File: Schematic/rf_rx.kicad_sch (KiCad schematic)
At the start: 12 parts, among them SW2 TS24CA, U1 ME6217C33M5G, U12 ESP-01F-2M, U13 E28-2G4M27SX

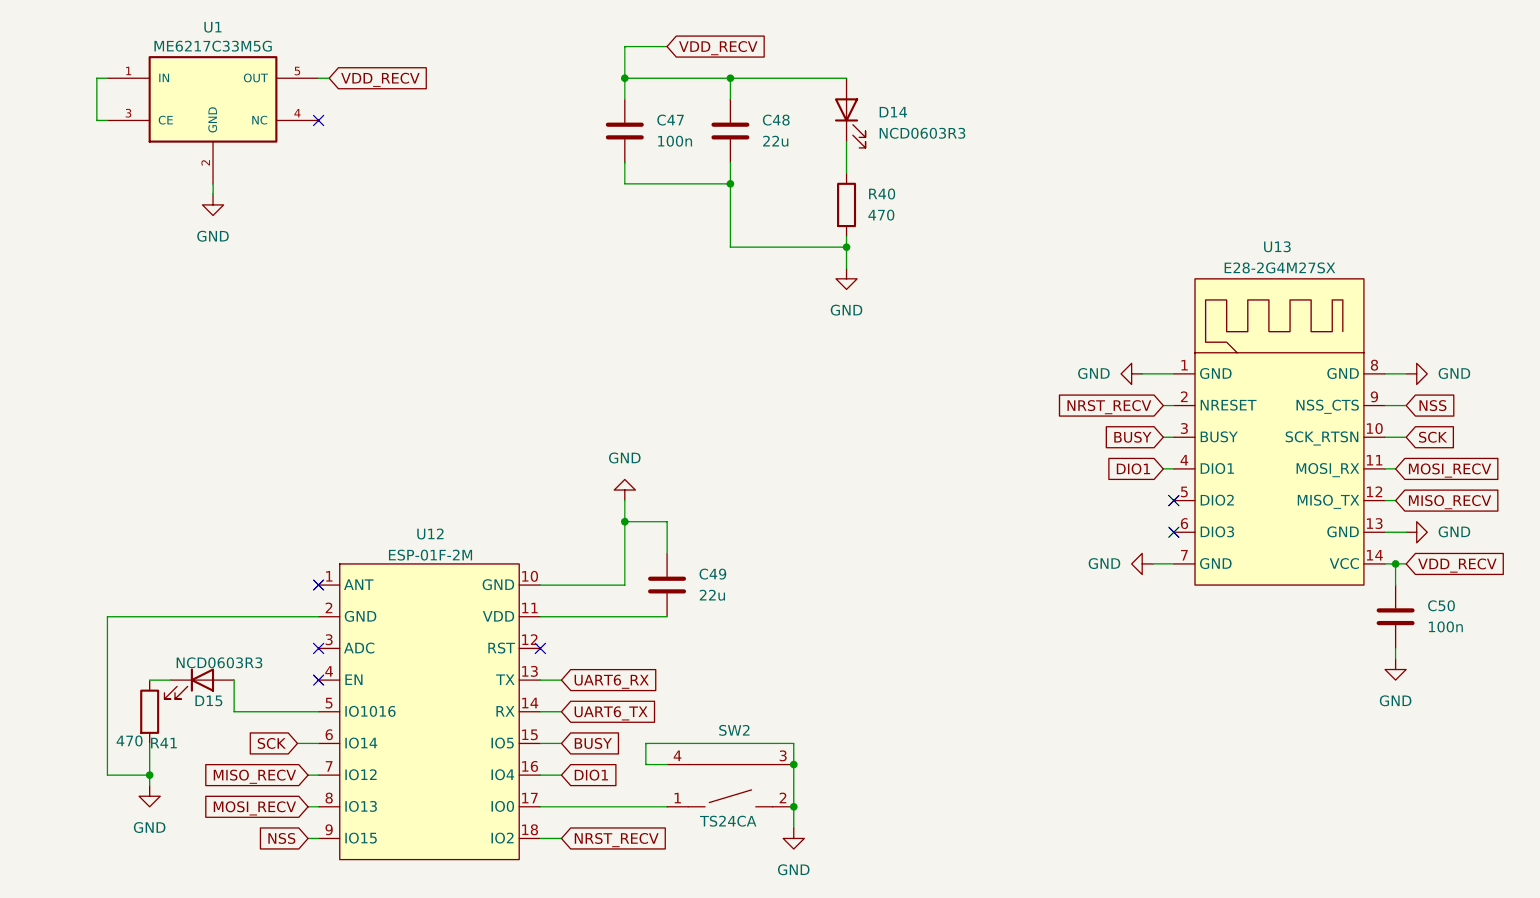
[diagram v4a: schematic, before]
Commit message: Refactor schematic files and update component placements
- Adjusted component positions in osd.kicad_sch for better layout.
- Added new junctions and wires in rf_rx.kicad_sch to improve connectivity.
- Introduced additional junctions and wires in sensors.kicad_sch for enhanced signal routing.
- Removed outdated backup file fch7-2025-11-18_191836.zip and added new backup fch7-2025-11-27_202230.zip.
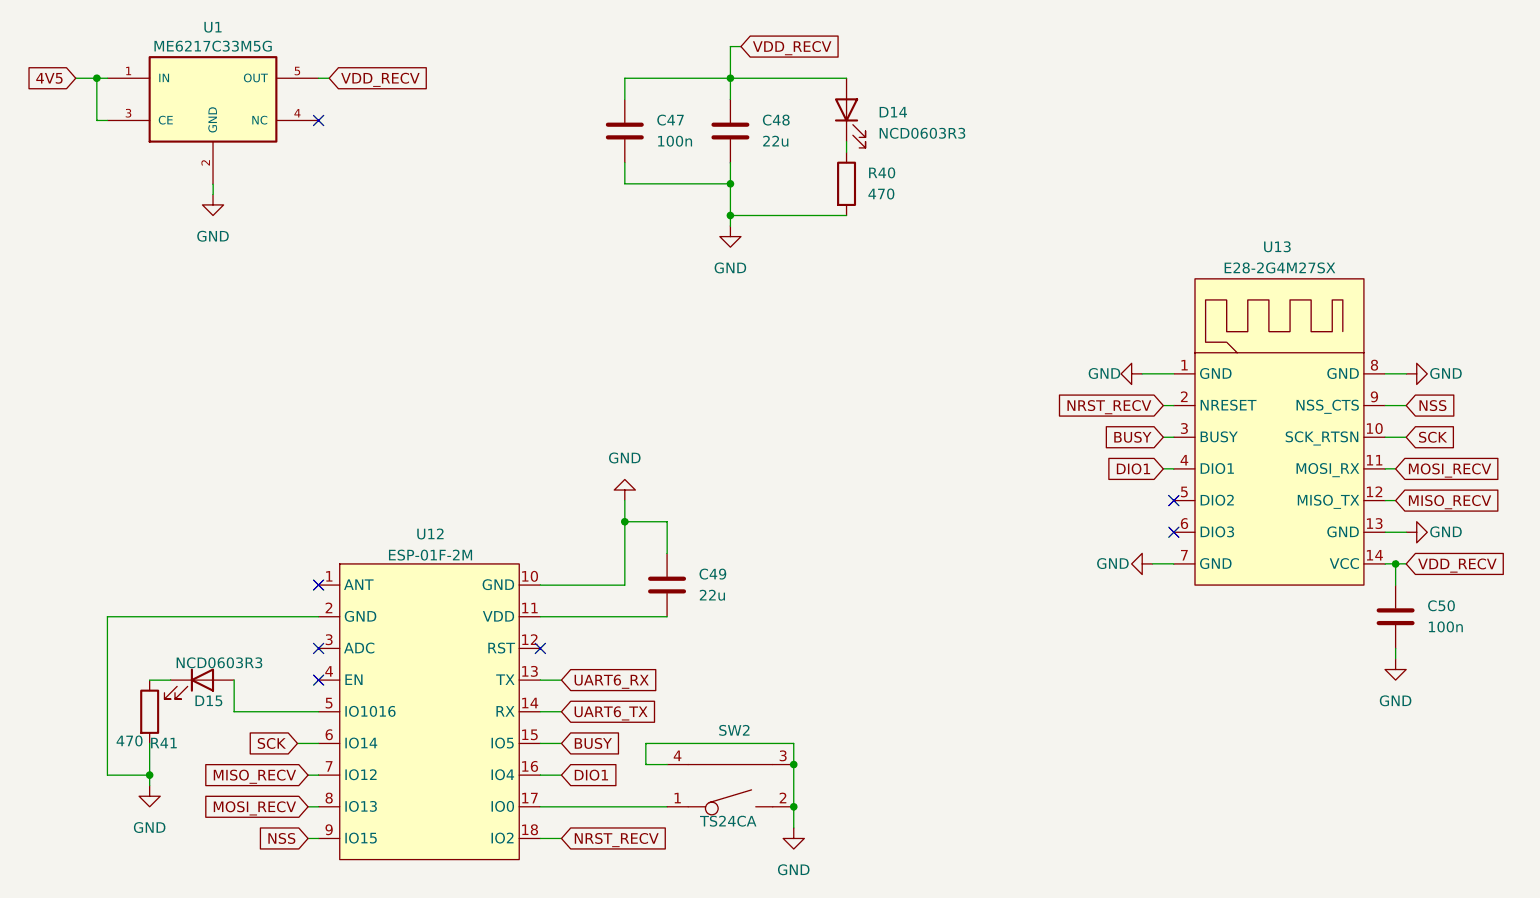
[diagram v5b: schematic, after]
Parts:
- SW2: footprint fch7_fp:SW-SMD_2P-TS24CA -> ProLib_pcs_2025-11-24:SW-SMD_2P-TS24CA
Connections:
- net 4V5: now reaches U1.1 (IN), U1.3 (CE)
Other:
- moved on the sheet: R40
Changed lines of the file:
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@@
 	(paper "A4")
+	(junction
+		(at 57.15 66.04)
+		(diameter 0)
+		(color 0 0 0 0)
+	)
+	(junction
+		(at 120.65 119.38)
+		(diameter 0)
+		(color 0 0 0 0)
+	)
+	(junction
+		(at 63.5 149.86)
+		(diameter 0)
+		(color 0 0 0 0)
+	)
+	(junction
+		(at 133.35 66.04)
+		(diameter 0)
+		(color 0 0 0 0)
+	)
+	(junction
+		(at 140.97 148.59)
+		(diameter 0)
+		(color 0 0 0 0)
+	)
+	(junction
+		(at 140.97 153.67)
+		(diameter 0)
+		(color 0 0 0 0)
+	)
+	(junction
+		(at 133.35 82.55)
+		(diameter 0)
+		(color 0 0 0 0)
+	)
+	(junction
+		(at 213.36 124.46)
+		(diameter 0)
+		(color 0 0 0 0)
+	)
 	(junction
 		(at 133.35 78.74)
@@
 		(color 0 0 0 0)
 	)
-	(junction
-		(at 147.32 86.36)
-		(diameter 0)
-		(color 0 0 0 0)
-	)
-	(junction
-		(at 120.65 119.38)
-		(diameter 0)
-		(color 0 0 0 0)
-	)
-	(junction
-		(at 63.5 149.86)
-		(diameter 0)
-		(color 0 0 0 0)
-	)
-	(junction
-		(at 133.35 66.04)
-		(diameter 0)
-		(color 0 0 0 0)
-	)
-	(junction
-		(at 120.65 66.04)
-		(diameter 0)
-		(color 0 0 0 0)
-	)
-	(junction
-		(at 140.97 148.59)
-		(diameter 0)
-		(color 0 0 0 0)
-	)
-	(junction
-		(at 140.97 153.67)
-		(diameter 0)
-		(color 0 0 0 0)
-	)
-	(junction
-		(at 213.36 124.46)
-		(diameter 0)
-		(color 0 0 0 0)
-	)
 	(no_connect
 		(at 110.49 134.62)
@@
 	(wire
 		(pts
-			(xy 133.35 78.74) (xy 133.35 86.36)
-		)
-		(stroke
-			(width 0)
-			(type default)
-		)
-	)
-	(wire
-		(pts
 			(xy 120.65 76.2) (xy 120.65 78.74)
 		)
@@
 	(wire
 		(pts
+			(xy 133.35 62.23) (xy 133.35 66.04)
+		)
+		(stroke
+			(width 0)
+			(type default)
+		)
+	)
+	(wire
+		(pts
 			(xy 82.55 149.86) (xy 83.82 149.86)
 		)
@@
 	(wire
 		(pts
-			(xy 147.32 85.09) (xy 147.32 86.36)
-		)
-		(stroke
-			(width 0)
-			(type default)
-		)
-	)
-	(wire
-		(pts
-			(xy 147.32 86.36) (xy 147.32 88.9)
+			(xy 134.62 62.23) (xy 133.35 62.23)
 		)
 		(stroke
@@
 	(wire
 		(pts
+			(xy 147.32 73.66) (xy 147.32 74.93)
+		)
+		(stroke
+			(width 0)
+			(type default)
+		)
+	)
+	(wire
+		(pts
 			(xy 57.15 66.04) (xy 57.15 71.12)
 		)
@@
 	(wire
 		(pts
-			(xy 125.73 62.23) (xy 120.65 62.23)
-		)
-		(stroke
-			(width 0)
-			(type default)
-		)
-	)
-	(wire
-		(pts
-			(xy 147.32 73.66) (xy 147.32 77.47)
-		)
-		(stroke
-			(width 0)
-			(type default)
-		)
-	)
-	(wire
-		(pts
 			(xy 82.55 153.67) (xy 83.82 153.67)
 		)
@@
 	(wire
 		(pts
+			(xy 133.35 82.55) (xy 133.35 78.74)
+		)
+		(stroke
+			(width 0)
+			(type default)
+		)
+	)
+	(wire
+		(pts
+			(xy 54.61 66.04) (xy 57.15 66.04)
+		)
+		(stroke
+			(width 0)
+			(type default)
+		)
+	)
+	(wire
+		(pts
 			(xy 212.09 109.22) (xy 214.63 109.22)
 		)
@@
 	(wire
 		(pts
-			(xy 133.35 86.36) (xy 147.32 86.36)
-		)
-		(stroke
-			(width 0)
-			(type default)
-		)
-	)
-	(wire
-		(pts
 			(xy 185.42 113.03) (xy 186.69 113.03)
 		)
@@
 	(wire
 		(pts
-			(xy 120.65 62.23) (xy 120.65 66.04)
-		)
-		(stroke
-			(width 0)
-			(type default)
-		)
-	)
-	(wire
-		(pts
 			(xy 110.49 138.43) (xy 113.03 138.43)
 		)
@@
 	(wire
 		(pts
+			(xy 147.32 82.55) (xy 133.35 82.55)
+		)
+		(stroke
+			(width 0)
+			(type default)
+		)
+	)
+	(wire
+		(pts
 			(xy 125.73 123.19) (xy 125.73 119.38)
 		)
@@
 		(pts
 			(xy 140.97 148.59) (xy 140.97 153.67)
+		)
+		(stroke
+			(width 0)
+			(type default)
+		)
+	)
+	(wire
+		(pts
+			(xy 133.35 82.55) (xy 133.35 83.82)
 		)
 		(stroke
@@
 		)
 	)
+	(global_label "4V5"
+		(shape input)
+		(at 54.61 66.04 180)
+		(fields_autoplaced yes)
+		(effects
+			(font
+				(size 1.27 1.27)
+			)
+			(justify right)
+		)
+		(property "Intersheetrefs" "${INTERSHEET_REFS}"
+			(at 48.1172 66.04 0)
+			(effects
+				(font
+					(size 1.27 1.27)
+				)
+				(justify right)
+				(hide yes)
+			)
+		)
+	)
 	(global_label "MOSI_RECV"
 		(shape input)
@@
 	(global_label "VDD_RECV"
 		(shape input)
-		(at 125.73 62.23 0)
+		(at 134.62 62.23 0)
 		(fields_autoplaced yes)
 		(effects
@@
 		)
 		(property "Intersheetrefs" "${INTERSHEET_REFS}"
-			(at 138.089 62.23 0)
+			(at 146.979 62.23 0)
 			(effects
 				(font
@@
 		(on_board yes)
 		(dnp no)
-		(fields_autoplaced yes)
 		(property "Reference" "#PWR048"
 			(at 177.8 124.46 0)
@@
 		)
 		(property "Value" "GND"
-			(at 180.34 124.4599 90)
+			(at 181.356 124.46 90)
 			(effects
 				(font
@@
 		(on_board yes)
 		(dnp no)
-		(fields_autoplaced yes)
 		(property "Reference" "#PWR047"
 			(at 176.53 101.6 0)
@@
 		)
 		(property "Value" "GND"
-			(at 179.07 101.5999 90)
+			(at 180.34 101.6 90)
 			(effects
 				(font
@@
 		(on_board yes)
 		(dnp no)
-		(fields_autoplaced yes)
 		(property "Reference" "#PWR050"
 			(at 220.98 101.6 0)
@@
 		)
 		(property "Value" "GND"
-			(at 218.44 101.5999 90)
+			(at 217.424 101.6 90)
 			(effects
 				(font
@@
 			)
 		)
-		(property "Footprint" "fch7_fp:SW-SMD_2P-TS24CA"
+		(property "Footprint" "ProLib_pcs_2025-11-24:SW-SMD_2P-TS24CA"
 			(at 132.588 144.526 0)
 			(effects
@@
 	(symbol
 		(lib_id "power:GND")
-		(at 147.32 88.9 0)
+		(at 133.35 83.82 0)
 		(unit 1)
 		(exclude_from_sim no)
@@
 		(fields_autoplaced yes)
 		(property "Reference" "#PWR043"
-			(at 147.32 95.25 0)
+			(at 133.35 90.17 0)
 			(effects
 				(font
@@
 		)
 		(property "Value" "GND"
-			(at 147.32 93.98 0)
+			(at 133.35 88.9 0)
 			(effects
 				(font
@@
 		)
 		(property "Footprint" ""
-			(at 147.32 88.9 0)
+			(at 133.35 83.82 0)
 			(effects
 				(font
@@
 		)
 		(property "Datasheet" ""
-			(at 147.32 88.9 0)
+			(at 133.35 83.82 0)
 			(effects
 				(font
@@
 		)
 		(property "Description" "Power symbol creates a global label with name \"GND\" , ground"
-			(at 147.32 88.9 0)
+			(at 133.35 83.82 0)
 			(effects
 				(font
@@
 	(symbol
 		(lib_id "Device:R")
-		(at 147.32 81.28 0)
+		(at 147.32 78.74 0)
 		(unit 1)
 		(exclude_from_sim no)
@@
 		(fields_autoplaced yes)
 		(property "Reference" "R40"
+			(at 149.86 77.4699 0)
+			(effects
+				(font
+					(size 1.27 1.27)
+				)
+				(justify left)
+			)
+		)
+		(property "Value" "470"
 			(at 149.86 80.0099 0)
 			(effects
@@
 			)
 		)
-		(property "Value" "470"
-			(at 149.86 82.5499 0)
-			(effects
-				(font
-					(size 1.27 1.27)
-				)
-				(justify left)
-			)
-		)
 		(property "Footprint" "Resistor_SMD:R_0603_1608Metric"
-			(at 145.542 81.28 90)
+			(at 145.542 78.74 90)
 			(effects
 				(font
@@
 		)
 		(property "Datasheet" "https://www.lcsc.com/datasheet/C23179.pdf"
-			(at 147.32 81.28 0)
+			(at 147.32 78.74 0)
 			(effects
 				(font
@@
 		)
 		(property "Description" "Resistor"
-			(at 147.32 81.28 0)
+			(at 147.32 78.74 0)
 			(effects
 				(font
@@
 		)
 		(property "Fréquence" ""
-			(at 147.32 81.28 0)
+			(at 147.32 78.74 0)
 			(effects
 				(font
@@
 		)
 		(property "MPN" "0603WAF4700T5E"
-			(at 147.32 81.28 0)
+			(at 147.32 78.74 0)
 			(effects
 				(font
@@
 		)
 		(property "Manufacturer" "UNI-ROYAL"
-			(at 147.32 81.28 0)
+			(at 147.32 78.74 0)
 			(effects
 				(font
@@
 		(on_board yes)
 		(dnp no)
-		(fields_autoplaced yes)
 		(property "Reference" "#PWR049"
 			(at 220.98 120.65 0)
@@
 		)
 		(property "Value" "GND"
-			(at 218.44 120.6499 90)
-			(effects
-				(font
+			(at 217.424 120.65 90)
+			(effects
+				(font

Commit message: Refactor code structure for improved readability and maintainability
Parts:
- SW2: footprint ProLib_pcs_2025-11-24:SW-SMD_2P-TS24CA -> fch7_fp:SW-SMD_2P-TS24CA
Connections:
- net VDD_RECV: now also C49.2, U12.11 (VDD)
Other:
- note added: "2.4Ghz wifi rf module"
- note added: "3.3V regulator for power supply net separated for RF modules"
- note added: "Decoupling and indicator LED"
- note added: "ELRS RX"
- moved on the sheet: C47, C48, C49, C50, D14, D15, R40, R41, SW2, U1, U12, U13

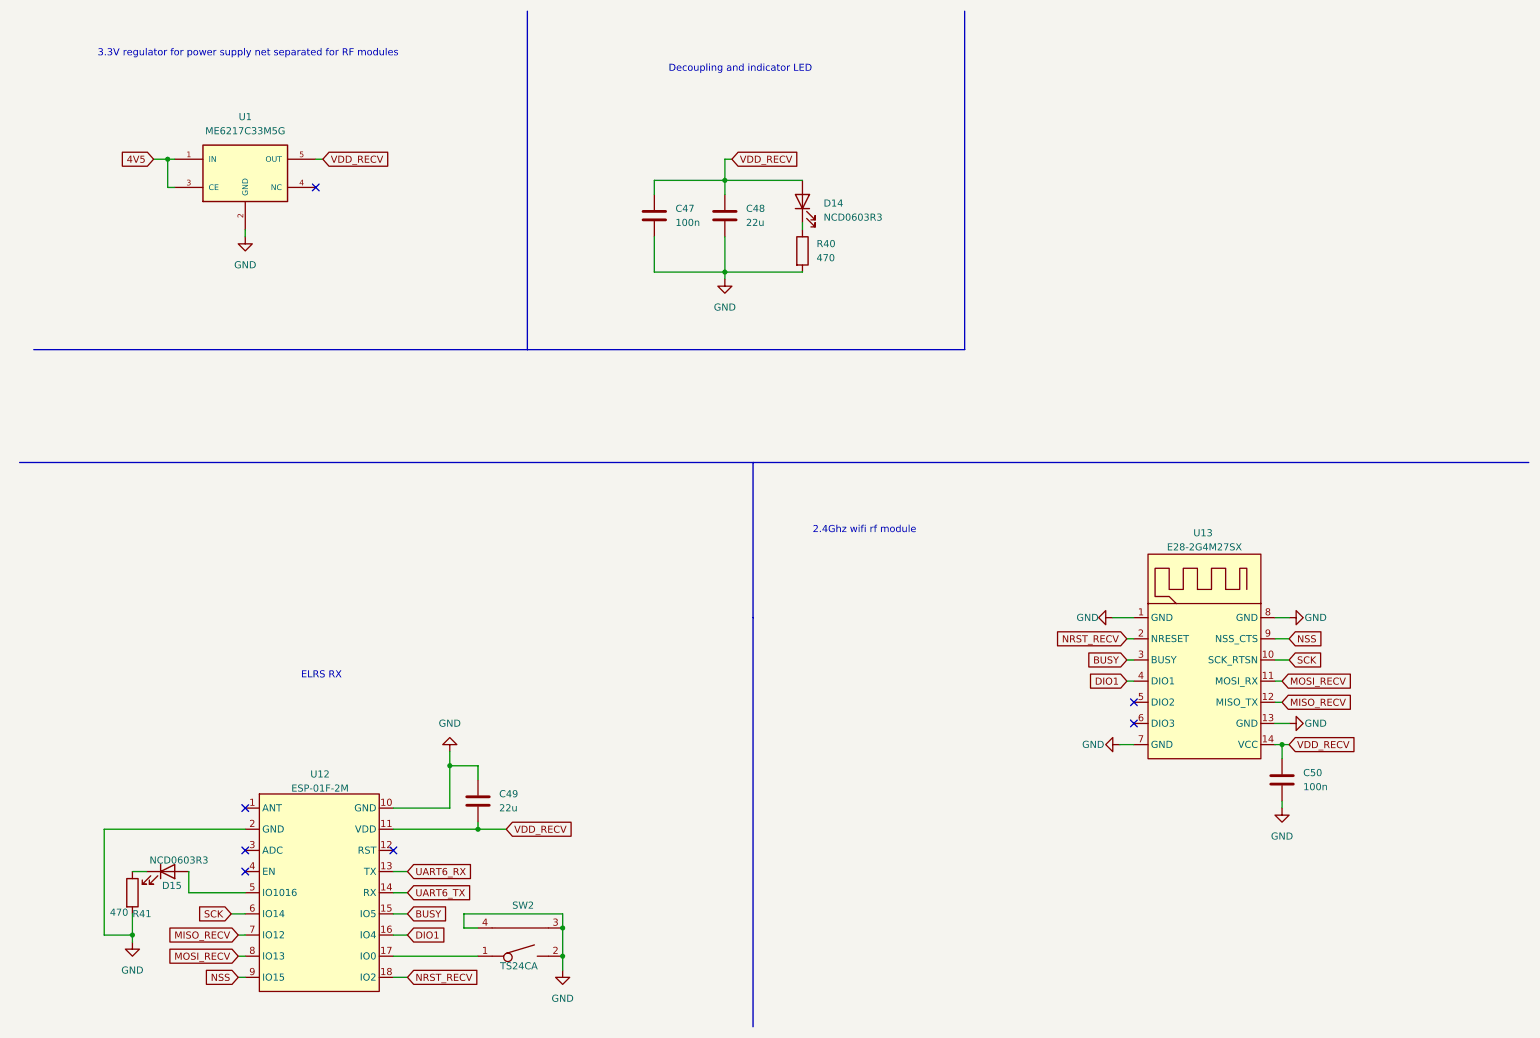
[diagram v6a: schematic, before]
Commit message: Removed useless analog OSD and VTX conneections to support only digital DJI
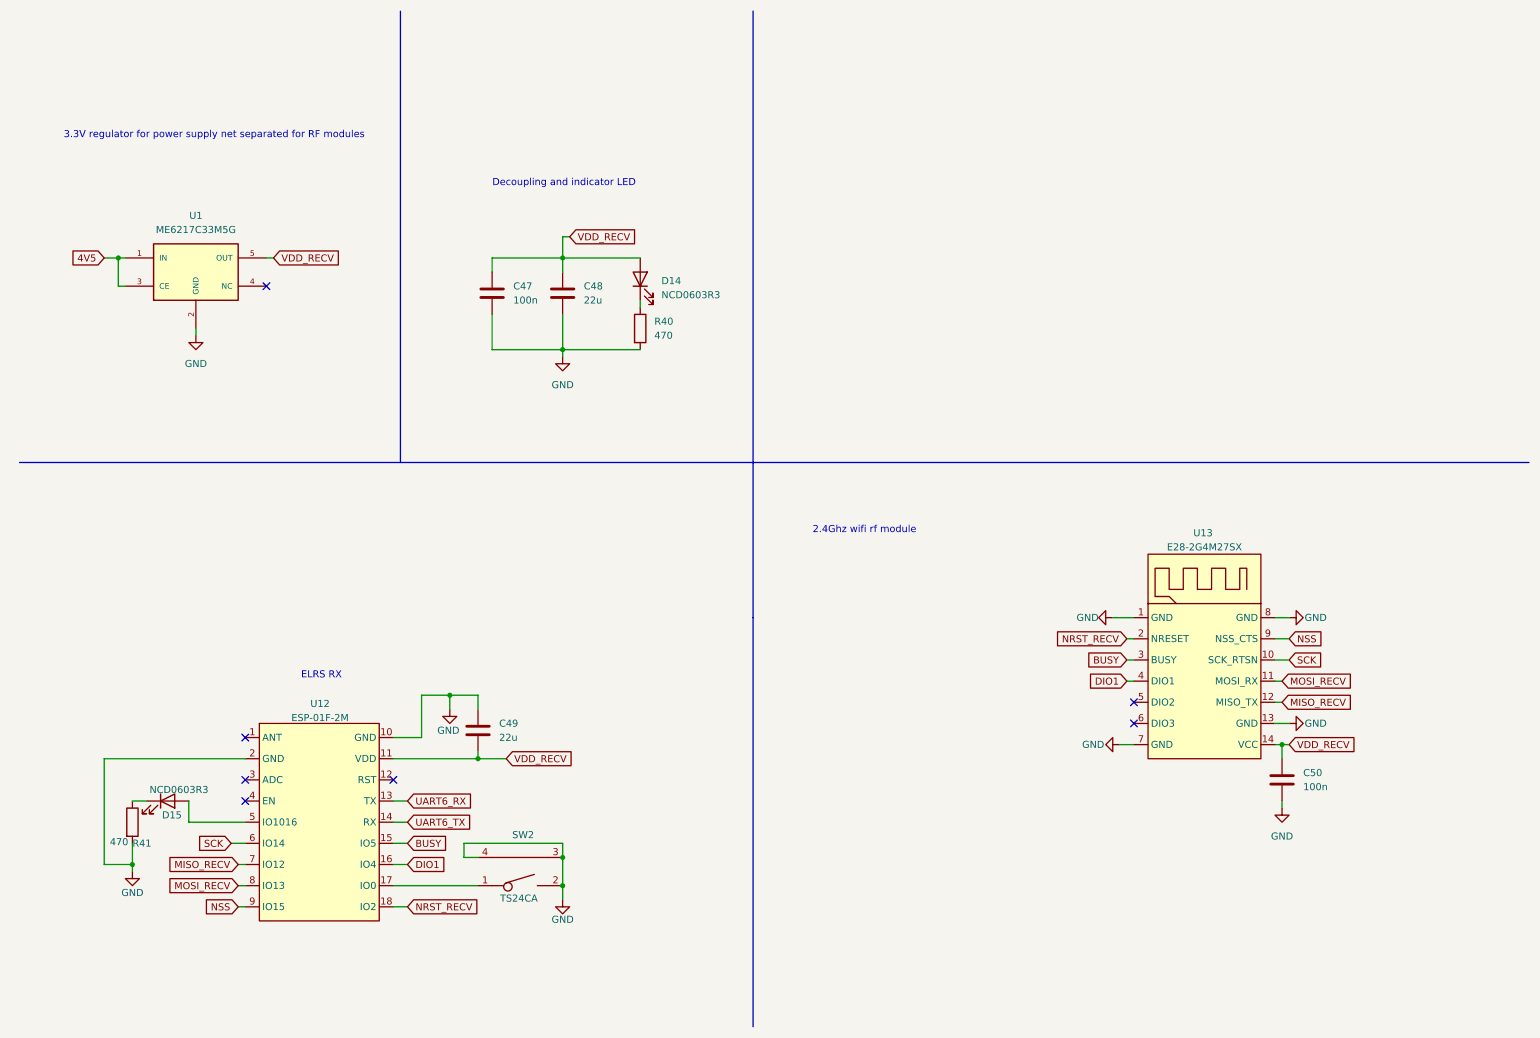
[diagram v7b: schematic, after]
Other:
- moved on the sheet: C47, C48, C49, D14, D15, R40, R41, SW2, U1, U12
